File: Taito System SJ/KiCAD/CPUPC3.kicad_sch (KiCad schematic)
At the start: 35 parts, among them U22 74LS86, U29 74LS367, U30 74LS367, U31 74LS367, U33 74LS83, U34 74LS08, U35 74LS32, U36 74LS04, U4 74LS374, U42 74LS374, U43 74LS374, U44 74LS374, U46 74LS83, U47 74LS83, U48 74LS367, U49 74LS367, U5 74LS374, U50 74LS367, U56 RAM_2016, U57 RAM_2016, U58 74LS83, U59 74LS83, U6 74LS374, U60 74LS374, U61 74LS02, U70 74LS157, U71 74LS157, U72 NEC_UPD2114, U73 NEC_UPD2114, U79 74LS04, U80 74LS157, U81 74LS157, U82 74LS157, U83 74LS174, U94 74LS32

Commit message: Multiple updates while coding core
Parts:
- added U45 (x2): 74LS367, symbol jt74:74LS367
- added U7: 74LS374, symbol jt74:74LS374
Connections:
- net CD0: now also U45.13 (O6b), U7.3 (D0)
- net CD1: now also U45.11 (O5b), U7.4 (D1)
- net CD2: now also U45.7 (O3a), U7.7 (D2)
- net CD3: now also U45.3 (O1a), U7.8 (D3)
- net CD4: now also U45.11 (O5b), U7.13 (D4)
- net CD5: now also U45.9 (O4a), U7.14 (D5)
- net CD6: now also U45.5 (O2a), U7.17 (D6)
- net CD7: now also U45.13 (O6b), U7.18 (D7)
- net D0: now also U45.14 (I6), U7.19 (O7)
- net D1: now also U45.12 (I5), U7.16 (O6)
- net D2: now also U45.6 (I3), U7.15 (O5)
- net D3: now also U45.2 (I1), U7.12 (O4)
- net D4: now also U45.12 (I5), U7.9 (O3)
- net D5: now also U45.10 (I4), U7.6 (O2)
- net D6: now also U45.4 (I2), U7.5 (O1)
- net D7: now also U45.14 (I6), U7.2 (O0)
- net ~{PH1}: now also U7.11 (Cp)
- net ~{RDA}: now also U7.1 (~{OE})
- net ~{1V'} renamed 1V'
- net ~{2V'} renamed 2V'
- net ~{4V'} renamed 4V'
- new net ~{WRA}: U45.1 (OEa), U45.15 (OEb), U45.15 (OEb)
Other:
- note added: "Horizontal Character Shift Registers A value of 1 will shift the playfield left by 1 tile as this offsets the memory address stored in U56 & U57."
- note added: "This seems to scroll vertical slices (every 8 pixels)"
- note added: "Vertical Character Scroll Registers"

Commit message: Tidied up loose ends
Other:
- note added: "Select layer based on 4HN/2HN"
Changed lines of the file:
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@@
+    (effects (font (size 1.27 1.27)) (justify left bottom))
+  )
+  (text "Select layer based on\n4HN/2HN" (at 292.1 307.34 0)
     (effects (font (size 1.27 1.27)) (justify left bottom))
   )

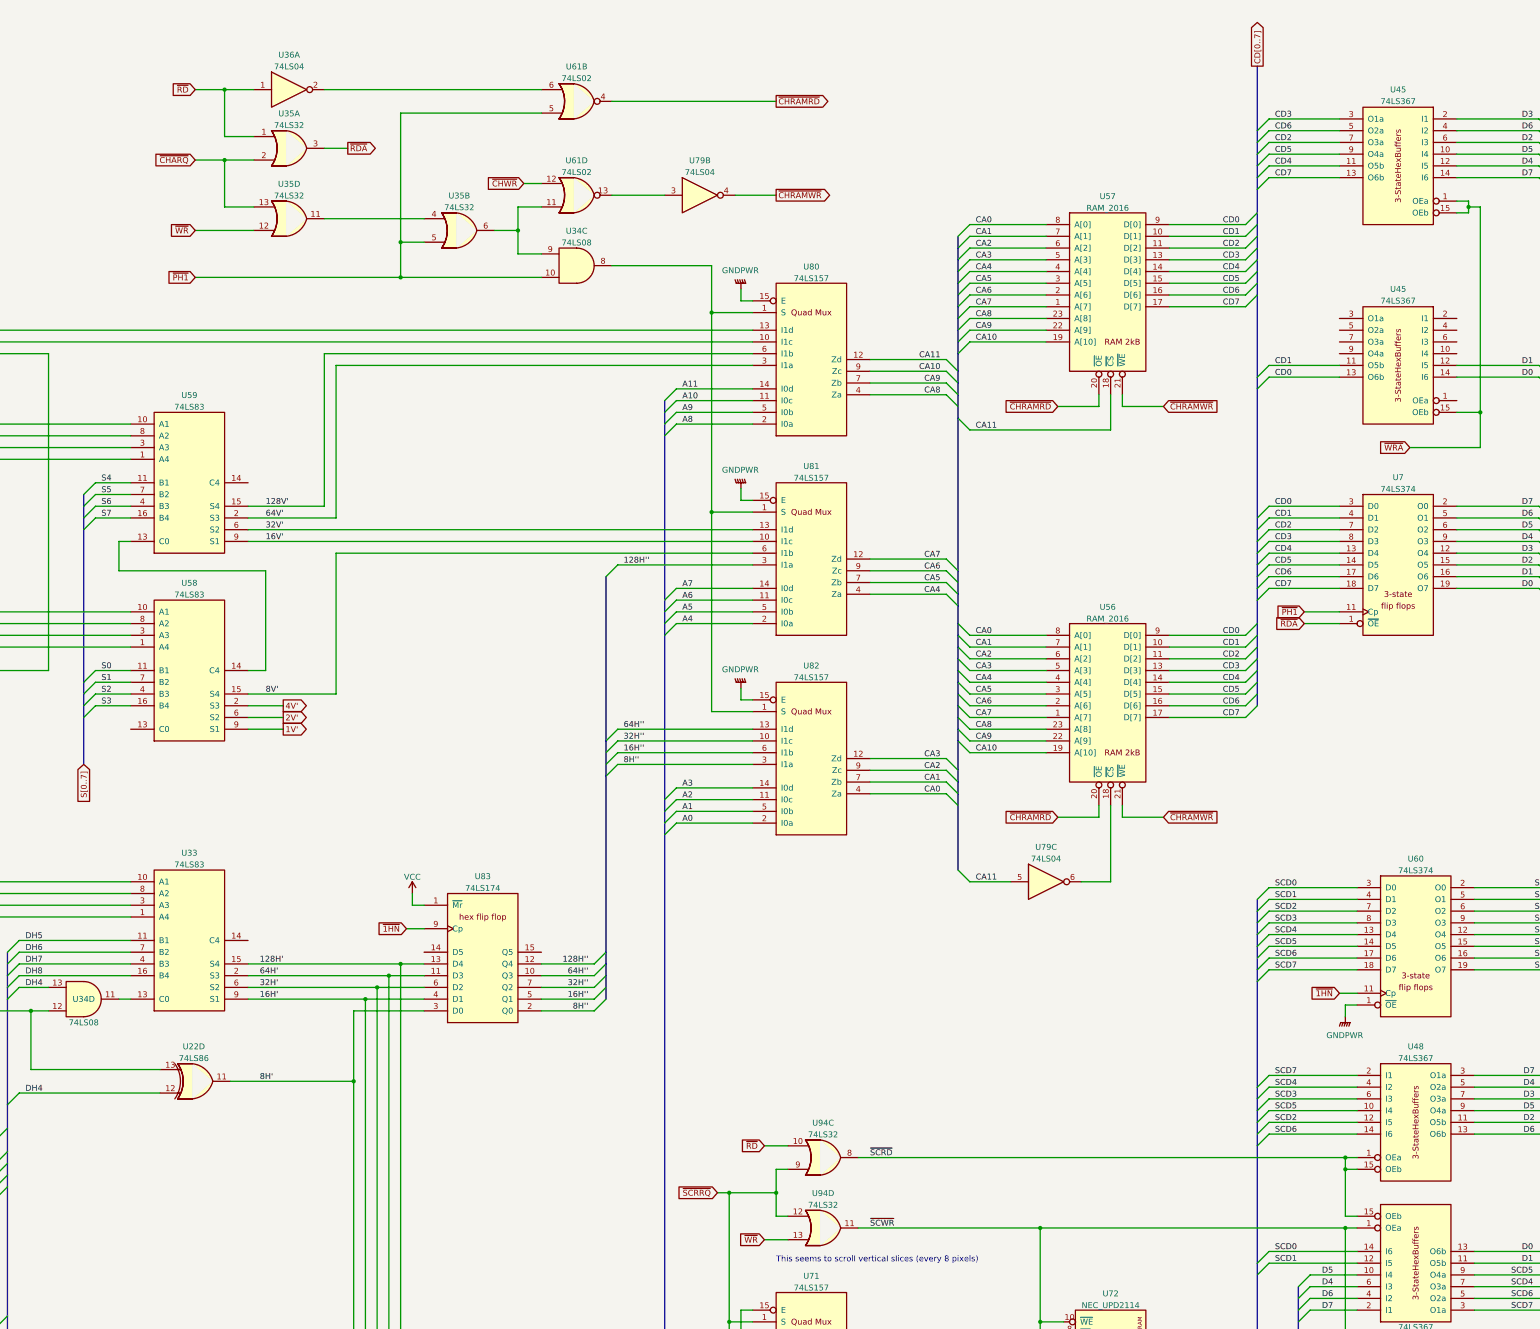
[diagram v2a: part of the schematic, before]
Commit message: Added MCU to Taito SJ Schematics
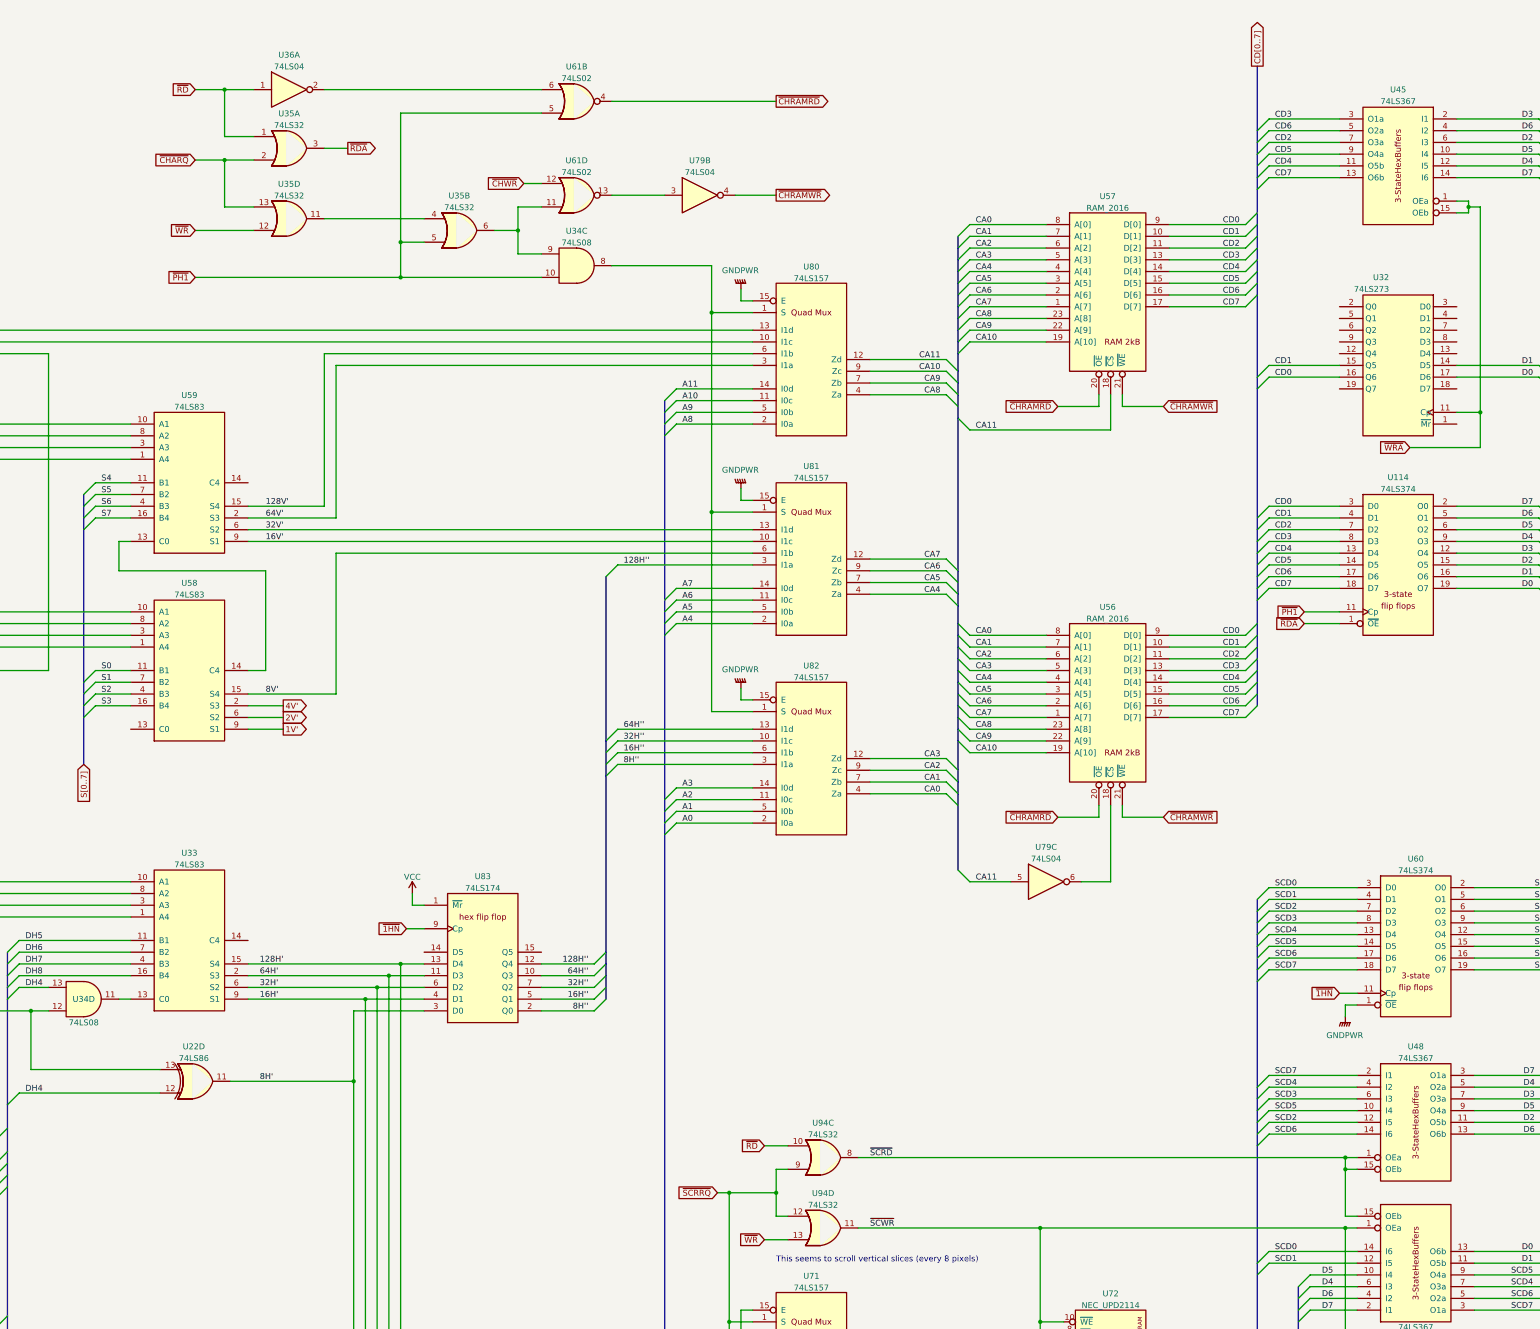
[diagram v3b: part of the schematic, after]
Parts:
- U32: renamed from U45; value 74LS367 -> 74LS273
- renumbered U7 to U114
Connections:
- net CD0: now also U32.16 (Q6); no longer U32.13 (O6b)
- net CD1: now also U32.15 (Q5); no longer U32.11 (O5b)
- net D0: now also U32.17 (D6); no longer U32.14 (I6)
- net D1: now also U32.14 (D5); no longer U32.12 (I5)
- net VCC: now also U32.20 (VCC)
- net ~{WRA}: now also U32.11 (Cp); no longer U32.15 (OEb)
- net GND: now reaches U32.10 (GND)
